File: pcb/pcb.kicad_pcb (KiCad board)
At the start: 2 copper layers, 70 x 70 mm, 65 parts, among them J1 USB_C_Receptacle_USB2.0, SW1 SW_Push, SW2 SW_Push, U1 SRV05-4, U2 XC6206P332MR, U3 DRV5056A3xDBZxQ1, U4 DRV5056A3xDBZxQ1, U5 DRV5056A3xDBZxQ1, U6 74AHCT1G125, U7 74AHCT1G125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

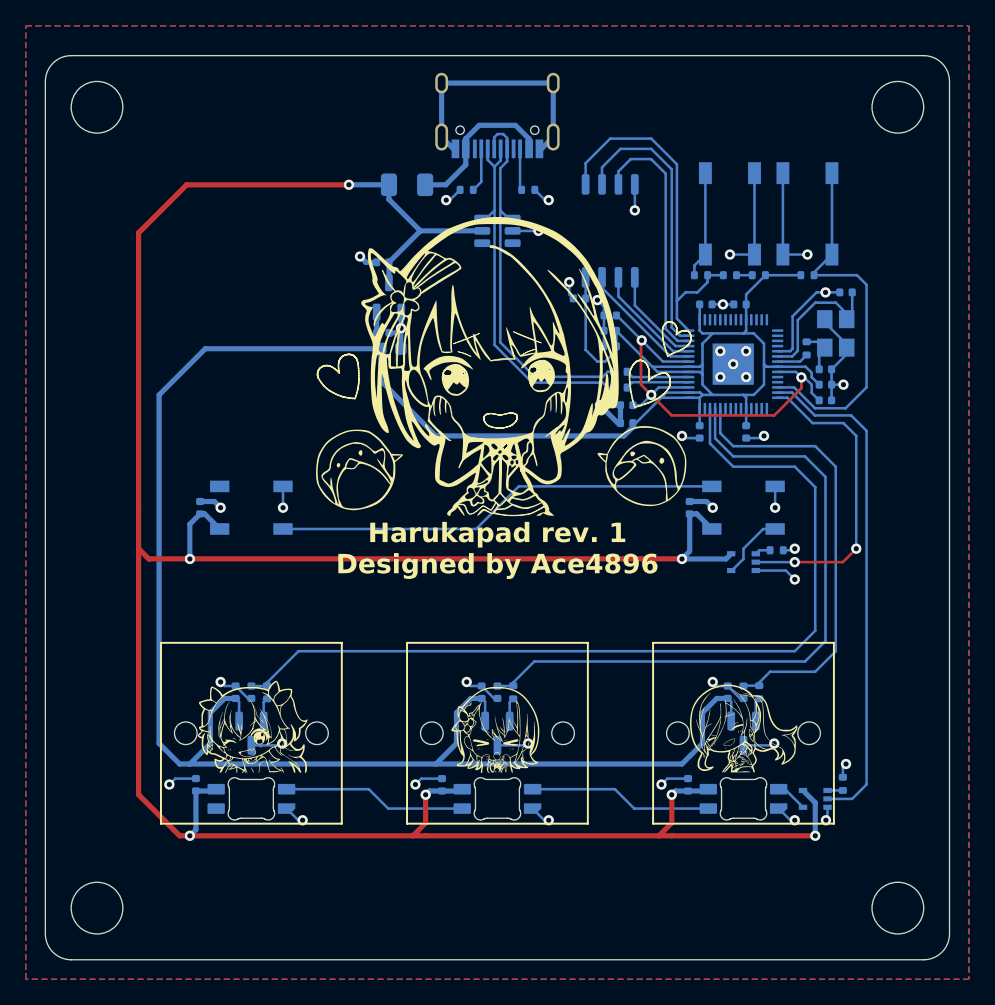
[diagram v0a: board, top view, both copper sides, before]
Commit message: fix: use grounded 3.5mm mounting holes on pcb didn't realise that the pads are used for grounding... definitely worth adding them in.
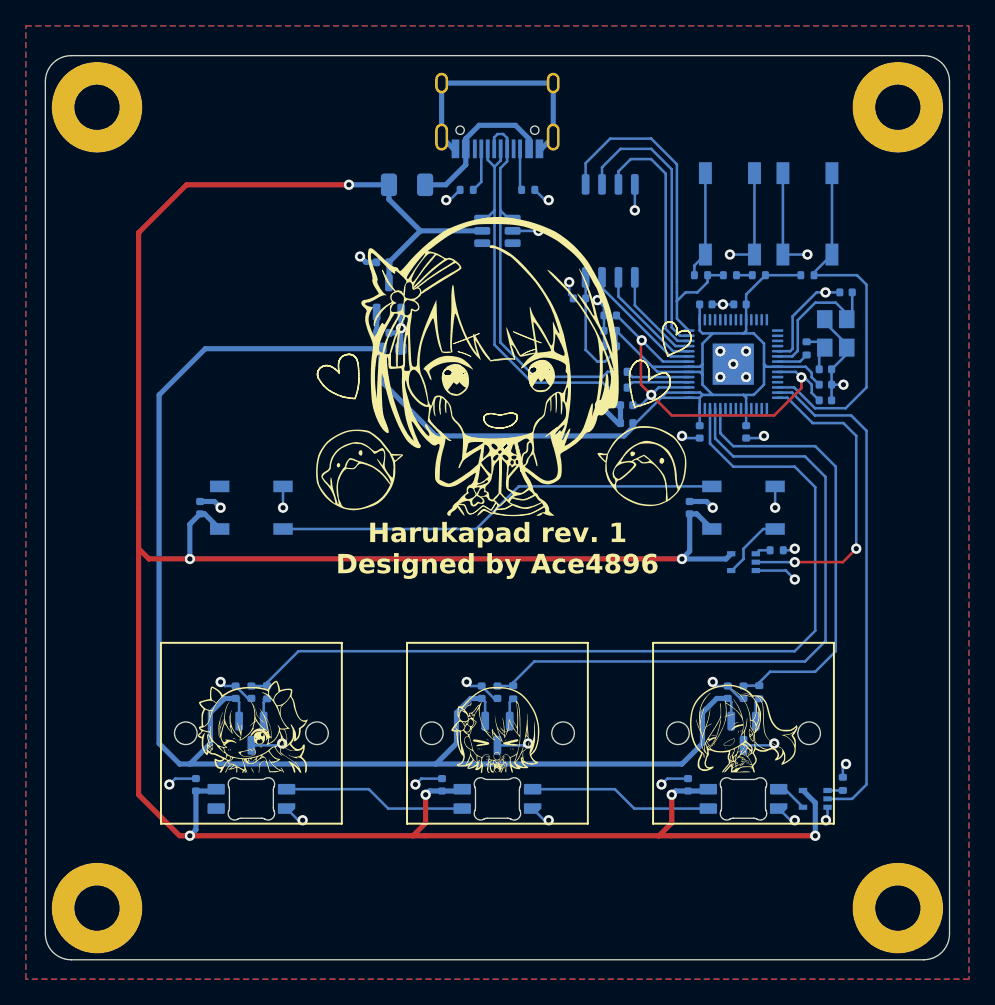
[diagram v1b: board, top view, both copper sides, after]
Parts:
- H1, H2, H3, H4: footprint MountingHole:MountingHole_4mm -> MountingHole:MountingHole_3.5mm_Pad
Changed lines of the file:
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@@
   (net 70 "Q_IO2")
   (net 71 "Q_IO1")
-  (footprint "MountingHole:MountingHole_4mm" locked (layer "F.Cu")
+  (footprint "MountingHole:MountingHole_3.5mm_Pad" locked (layer "F.Cu")
     (at 19.8 19.8)
-    (descr "Mounting Hole 4mm, no annular")
-    (tags "mounting hole 4mm no annular")
+    (descr "Mounting Hole 3.5mm")
+    (tags "mounting hole 3.5mm")
     (property "LCSC" "")
     (property "Sheetfile" "pcb.kicad_sch")
@@
     (property "ki_keywords" "mounting hole")
     (attr exclude_from_pos_files exclude_from_bom)
-    (fp_text reference "H1" (at 0 -5) (layer "F.SilkS") hide
-        (effects (font (size 1 0.8) (thickness 0.15)))
-    )
-    (fp_text value "Mounting Hole" (at 0 5 unlocked) (layer "F.Fab")
+    (fp_text reference "H1" (at 0 -4.5) (layer "F.SilkS") hide
         (effects (font (size 1 1) (thickness 0.15)))
     )
-    (fp_text user "${REFERENCE}" (at 0 0 unlocked) (layer "F.Fab")
+    (fp_text value "Mounting Hole" (at 0 4.5) (layer "F.Fab")
         (effects (font (size 1 1) (thickness 0.15)))
     )
-    (fp_circle (center 0 0) (end 4 0)
+    (fp_text user "${REFERENCE}" (at 0 0) (layer "F.Fab")
+        (effects (font (size 1 1) (thickness 0.15)))
+    )
+    (fp_circle (center 0 0) (end 3.5 0)
       (stroke (width 0.15) (type solid)) (fill none) (layer "Cmts.User"))
-    (fp_circle (center 0 0) (end 4.25 0)
+    (fp_circle (center 0 0) (end 3.75 0)
       (stroke (width 0.05) (type solid)) (fill none) (layer "F.CrtYd"))
-    (pad "" np_thru_hole circle locked (at 0 0) (size 4 4) (drill 4) (layers "*.Cu" "*.Mask"))
+    (pad "1" thru_hole circle locked (at 0 0) (size 7 7) (drill 3.5) (layers "*.Cu" "*.Mask"))
   )
-  (footprint "MountingHole:MountingHole_4mm" locked (layer "F.Cu")
+  (footprint "MountingHole:MountingHole_3.5mm_Pad" locked (layer "F.Cu")
     (at 81.8 19.8)
-    (descr "Mounting Hole 4mm, no annular")
-    (tags "mounting hole 4mm no annular")
+    (descr "Mounting Hole 3.5mm")
+    (tags "mounting hole 3.5mm")
     (property "LCSC" "")
     (property "Sheetfile" "pcb.kicad_sch")
@@
     (property "ki_keywords" "mounting hole")
     (attr exclude_from_pos_files exclude_from_bom)
-    (fp_text reference "H2" (at 0 -5) (layer "F.SilkS") hide
-        (effects (font (size 1 0.8) (thickness 0.15)))
-    )
-    (fp_text value "Mounting Hole" (at 0 5 unlocked) (layer "F.Fab")
+    (fp_text reference "H2" (at 0 -4.5) (layer "F.SilkS") hide
         (effects (font (size 1 1) (thickness 0.15)))
     )
-    (fp_text user "${REFERENCE}" (at 0 0 unlocked) (layer "F.Fab")
+    (fp_text value "Mounting Hole" (at 0 4.5) (layer "F.Fab")
         (effects (font (size 1 1) (thickness 0.15)))
     )
-    (fp_circle (center 0 0) (end 4 0)
+    (fp_text user "${REFERENCE}" (at 0 0) (layer "F.Fab")
+        (effects (font (size 1 1) (thickness 0.15)))
+    )
+    (fp_circle (center 0 0) (end 3.5 0)
       (stroke (width 0.15) (type solid)) (fill none) (layer "Cmts.User"))
-    (fp_circle (center 0 0) (end 4.25 0)
+    (fp_circle (center 0 0) (end 3.75 0)
       (stroke (width 0.05) (type solid)) (fill none) (layer "F.CrtYd"))
-    (pad "" np_thru_hole circle locked (at 0 0) (size 4 4) (drill 4) (layers "*.Cu" "*.Mask"))
+    (pad "1" thru_hole circle locked (at 0 0) (size 7 7) (drill 3.5) (layers "*.Cu" "*.Mask"))
   )
-  (footprint "MountingHole:MountingHole_4mm" locked (layer "F.Cu")
+  (footprint "MountingHole:MountingHole_3.5mm_Pad" locked (layer "F.Cu")
     (at 19.8 81.8)
-    (descr "Mounting Hole 4mm, no annular")
-    (tags "mounting hole 4mm no annular")
+    (descr "Mounting Hole 3.5mm")
+    (tags "mounting hole 3.5mm")
     (property "LCSC" "")
     (property "Sheetfile" "pcb.kicad_sch")
@@
     (property "ki_keywords" "mounting hole")
     (attr exclude_from_pos_files exclude_from_bom)
-    (fp_text reference "H3" (at 0 -5) (layer "F.SilkS") hide
-        (effects (font (size 1 0.8) (thickness 0.15)))
-    )
-    (fp_text value "Mounting Hole" (at 0 5 unlocked) (layer "F.Fab")
+    (fp_text reference "H3" (at 0 -4.5) (layer "F.SilkS") hide
         (effects (font (size 1 1) (thickness 0.15)))
     )
-    (fp_text user "${REFERENCE}" (at 0 0 unlocked) (layer "F.Fab")
+    (fp_text value "Mounting Hole" (at 0 4.5) (layer "F.Fab")
         (effects (font (size 1 1) (thickness 0.15)))
     )
-    (fp_circle (center 0 0) (end 4 0)
+    (fp_text user "${REFERENCE}" (at 0 0) (layer "F.Fab")
+        (effects (font (size 1 1) (thickness 0.15)))
+    )
+    (fp_circle (center 0 0) (end 3.5 0)
       (stroke (width 0.15) (type solid)) (fill none) (layer "Cmts.User"))
-    (fp_circle (center 0 0) (end 4.25 0)
+    (fp_circle (center 0 0) (end 3.75 0)
       (stroke (width 0.05) (type solid)) (fill none) (layer "F.CrtYd"))
-    (pad "" np_thru_hole circle locked (at 0 0) (size 4 4) (drill 4) (layers "*.Cu" "*.Mask"))
+    (pad "1" thru_hole circle locked (at 0 0) (size 7 7) (drill 3.5) (layers "*.Cu" "*.Mask"))
   )
-  (footprint "MountingHole:MountingHole_4mm" locked (layer "F.Cu")
+  (footprint "MountingHole:MountingHole_3.5mm_Pad" locked (layer "F.Cu")
     (at 81.8 81.8)
-    (descr "Mounting Hole 4mm, no annular")
-    (tags "mounting hole 4mm no annular")
+    (descr "Mounting Hole 3.5mm")
+    (tags "mounting hole 3.5mm")
     (property "LCSC" "")
     (property "Sheetfile" "pcb.kicad_sch")
@@
     (property "ki_keywords" "mounting hole")
     (attr exclude_from_pos_files exclude_from_bom)
-    (fp_text reference "H4" (at 0 -5) (layer "F.SilkS") hide
-        (effects (font (size 1 0.8) (thickness 0.15)))
-    )
-    (fp_text value "Mounting Hole" (at 0 5 unlocked) (layer "F.Fab")
+    (fp_text reference "H4" (at 0 -4.5) (layer "F.SilkS") hide
         (effects (font (size 1 1) (thickness 0.15)))
     )
-    (fp_text user "${REFERENCE}" (at 0 0 unlocked) (layer "F.Fab")
+    (fp_text value "Mounting Hole" (at 0 4.5) (layer "F.Fab")
         (effects (font (size 1 1) (thickness 0.15)))
     )
-    (fp_circle (center 0 0) (end 4 0)
+    (fp_text user "${REFERENCE}" (at 0 0) (layer "F.Fab")
+        (effects (font (size 1 1) (thickness 0.15)))
+    )
+    (fp_circle (center 0 0) (end 3.5 0)
       (stroke (width 0.15) (type solid)) (fill none) (layer "Cmts.User"))
-    (fp_circle (center 0 0) (end 4.25 0)
+    (fp_circle (center 0 0) (end 3.75 0)
       (stroke (width 0.05) (type solid)) (fill none) (layer "F.CrtYd"))
-    (pad "" np_thru_hole circle locked (at 0 0) (size 4 4) (drill 4) (layers "*.Cu" "*.Mask"))
+    (pad "1" thru_hole circle locked (at 0 0) (size 7 7) (drill 3.5) (layers "*.Cu" "*.Mask"))
   )
   (footprint "Package_SO:SOIC-8_5.23x5.23mm_P1.27mm" (layer "B.Cu")
